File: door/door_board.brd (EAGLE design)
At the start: 50.3 x 50 mm, 40 parts, among them IC1 MCP1703CB, IC2 MCP601OT, IC3 AP1609SOP8, Q1 4.3A/20V/54mΩ, T2 BC847

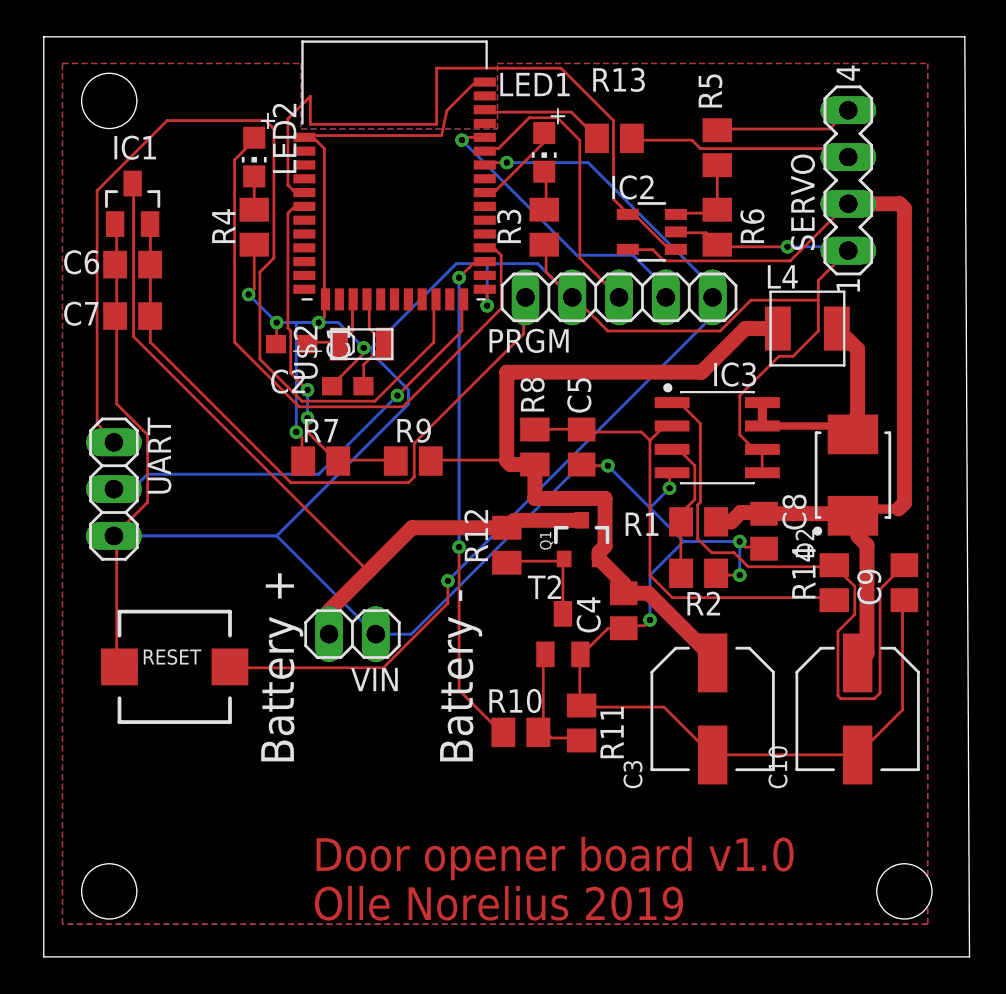
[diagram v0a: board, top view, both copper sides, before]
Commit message: Updated board to version 1.1
Fixed VCC to nrf
Flipped HV enable high side mosfet
Corrected AP1609 footprint
Updated board text
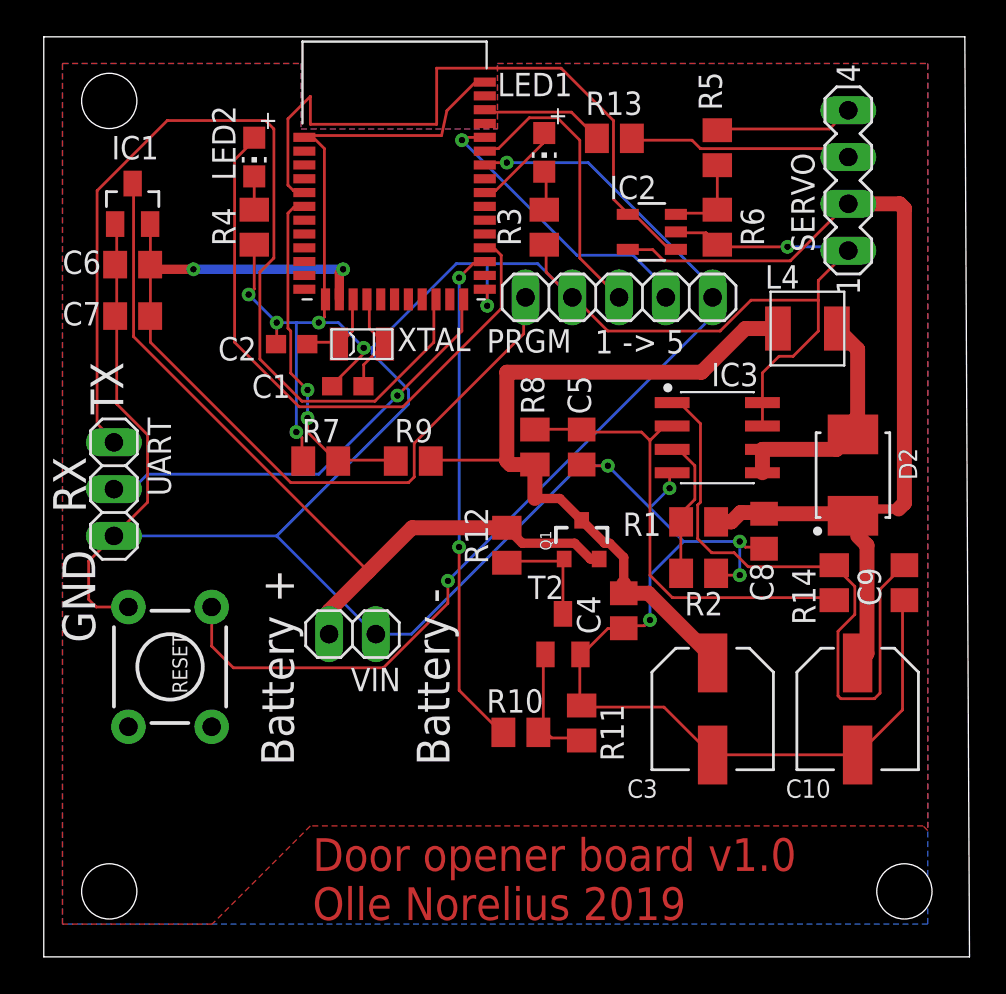
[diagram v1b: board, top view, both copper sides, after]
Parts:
- RESET: value (none) -> MOMENTARY-SWITCH-SPST-PTH-6.0MM; device adafruit:PUSHBUTTON_SMD_SJ -> SparkFun-Switches:TACTILE_SWITCH_PTH_6.0MM
- moved RESET 0.25 mm to (6.86, 15.7), turned to 270 degrees
- renumbered U$2 to XTAL
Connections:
- net N$4 renamed RX
- net N$5 renamed TX
- removed net VDD_NRF: U$1.P$26
- net 3V3: now also U$1.P$26
- net GND: now also IC3.7, IC3.8, RESET.3; no longer IC3.5, IC3.6, RESET.P$2
- net LX: now also IC3.5, IC3.6; no longer IC3.7, IC3.8
- net NRST: now also RESET.1; no longer RESET.P$1
- net VIN: now also Q1.2; no longer Q1.3
- net VIN_CONT: now also Q1.3; no longer Q1.2
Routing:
- net 3V3: track 36.4 -> 48.5 mm, vias 0 -> 2
- net GND: track 233.5 -> 228.8 mm
- net NRST: track 51.7 -> 55.2 mm
- net VIN: track 43.4 -> 44.9 mm
- net 5V: track 50.7 -> 52.0 mm
- net LX: track 11.9 -> 13.1 mm
- net VIN_CONT: track 44.4 -> 43.3 mm
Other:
- board text added: "1 -> 5"
- board text added: "GND"
- board text added: "RX"
- board text added: "TX"
